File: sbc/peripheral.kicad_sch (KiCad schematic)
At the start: 19 parts, among them J1 Controller-Connector, J2 Controller-Connector, J3 SIO-Header, J4 QTPY-RP2040, U12 TXU0104, U13 TXU0204

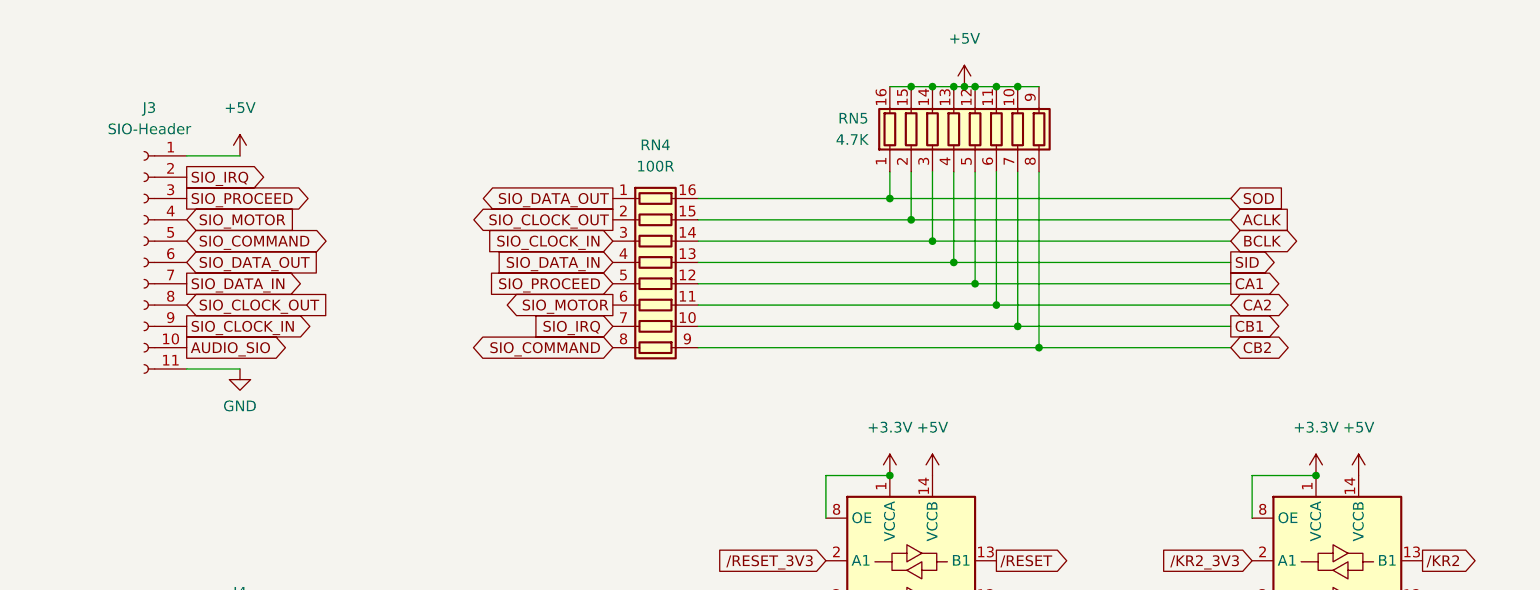
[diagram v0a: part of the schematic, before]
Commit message: SBC v1.1
PCB fixes/changes:

  - Permanently power voltage translators
  - Conservatively specified a slower SRAM (the previous/faster SRAM does actually work fine)
  - RMU: Speculatively provided unbuffered PHI0 input and OE output (not actually needed)
  - Add pullups to open drain GTIA outputs
  - Plot selected values on silk screen
  - Accommodate KiCad 7 upgrade

- PLD changes:
  - Fix AMU logic
  - Fix RMU (unbuffered PHI0 and OE output not needed)

- QTPY firmware:
  - add soft power on/off support (Ctrl-F12)
  - reflects switched power and usb state in the neopixel
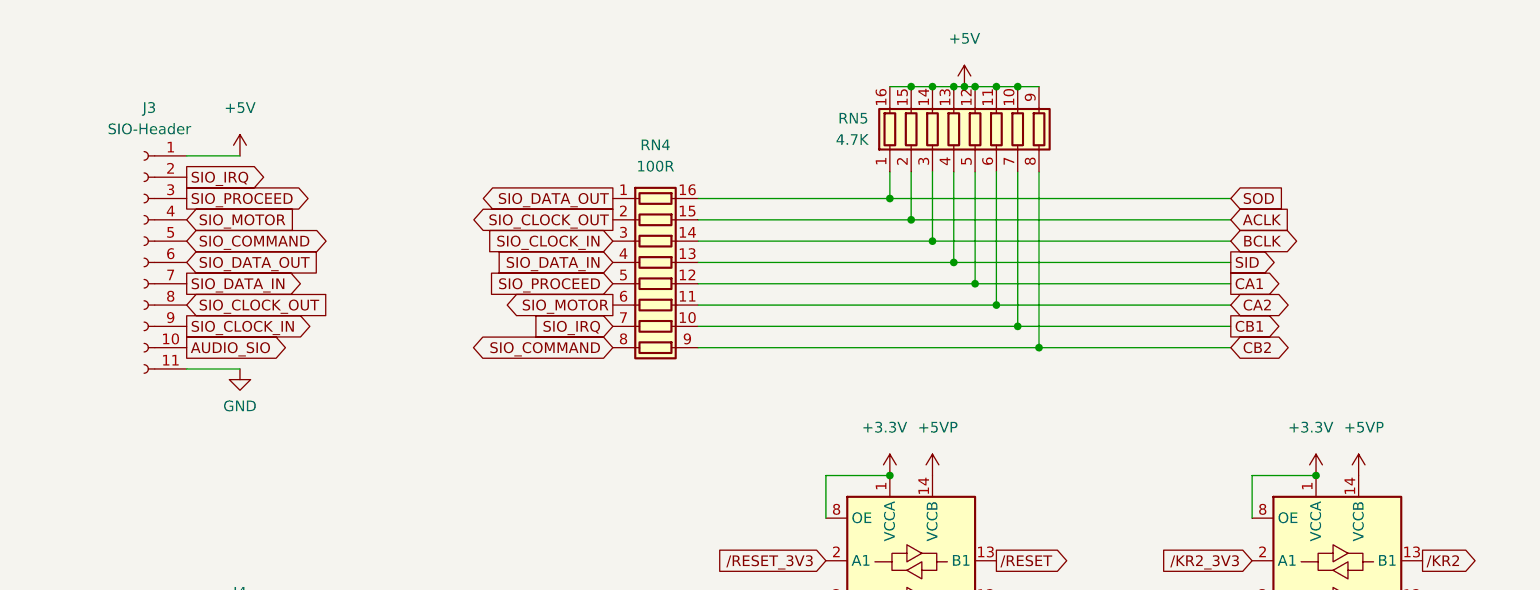
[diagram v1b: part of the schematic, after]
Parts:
- J1, J2: symbol Connector:DB9_Male_MountingHoles -> Connector:DE9_Plug_MountingHoles
- J3: symbol Connector:Conn_01x11_Female -> Connector:Conn_01x11_Socket
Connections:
- net +5V: no longer U12.14 (VCCB), U13.14 (VCCB)
- net +5VP: now also U12.14 (VCCB), U13.14 (VCCB)
- net +3V3 renamed +3.3V

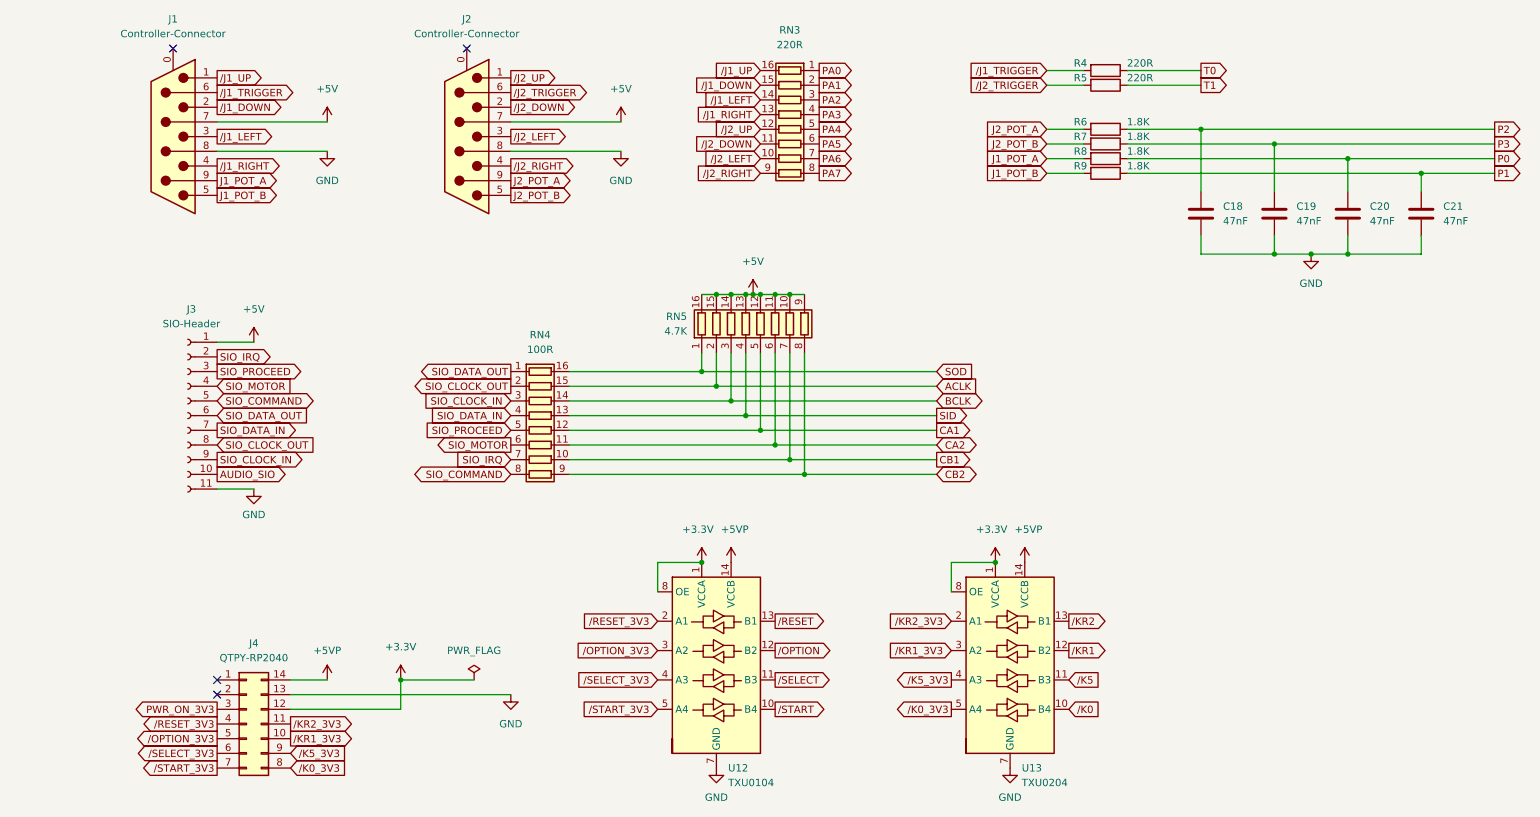
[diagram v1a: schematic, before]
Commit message: SBC v1.2
SBC fixes/changes:

  - S-Video:
    - Fix S-Video footprint (Y and C swapped, and GNDs swapped) and adapt schematic to match
    - Wire S-Video grounds to AVA header instead of directly to (digital) GND
  - Audio:
    - Wire Audio-Out ground to AVA header
    - Drop SIO audio
    - Pullup open drain pokey audio
  - AMU/RMU:
    - Connect ROM and RAM OE to GND
    - Reserve AMU pin for "IO"
    - Reserve RMU pin for "antic" (registered halt)
    - Support for separate Antic banking (clock RMU with /phi2)
    - Supoprt 130XE and 320XE (compy)
  - Add the option for a resistor between OSC, PHI0 buffer and PHI2 buffer (to reduce over/under-shoot)
  - Invert CA2 (a PNP transistor on the Atari 800 XL inverts this signal)

Additions:

  - SBC Audio/Video board
  - SBC Case
  - SBC SD board

Stylize the complete system as "SFF 320XE".
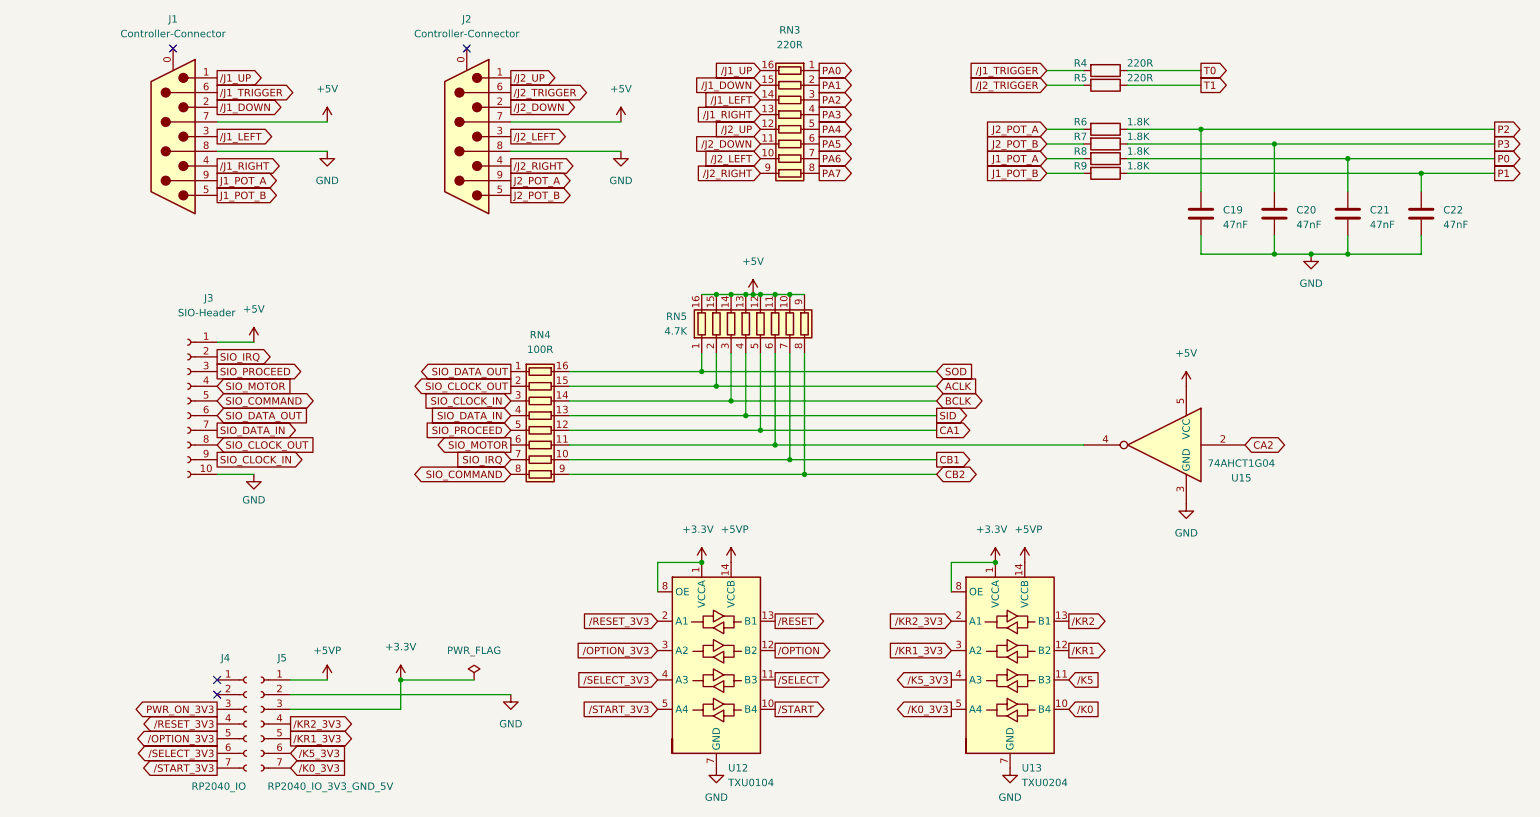
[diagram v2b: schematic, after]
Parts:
- removed J3: SIO-Header, Connector_PinSocket_2.54mm:PinSocket_1x11_P2.54mm_Vertical, symbol Connector:Conn_01x11_Socket
- removed J4: QTPY-RP2040, Package_DIP:DIP-14_W15.24mm, symbol Connector_Generic:Conn_02x07_Counter_Clockwise
- added J3: SIO-Header, Connector_PinSocket_2.54mm:PinSocket_1x10_P2.54mm_Vertical, symbol Connector:Conn_01x10_Socket
- added J4: RP2040_IO, Connector_PinSocket_2.54mm:PinSocket_1x07_P2.54mm_Vertical, symbol Connector:Conn_01x07_Socket
- added J5: RP2040_IO_3V3_GND_5V, Connector_PinSocket_2.54mm:PinSocket_1x07_P2.54mm_Vertical, symbol Connector:Conn_01x07_Socket
- added U15: 74AHCT1G04, Package_TO_SOT_SMD:SOT-23-5_HandSoldering, symbol 74xGxx:74AHCT1G04
- renumbered C18 to C19, C19 to C20, C20 to C21, C21 to C22
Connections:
- net +3.3V: now also J5.3 (Pin_3)
- net +5V: now also J3.1 (Pin_1), U15.5 (VCC)
- net +5VP: now also J5.1 (Pin_1)
- net CA2: now also U15.2; no longer RN4.11 (R6.2), RN5.6 (R6.1)
- net GND: now also J3.10 (Pin_10), J5.2 (Pin_2), U15.3 (GND)
- net PWR_ON_3V3: now also J4.3 (Pin_3)
- net SIO_CLOCK_IN: now also J3.9 (Pin_9)
- net SIO_CLOCK_OUT: now also J3.8 (Pin_8)
- net SIO_COMMAND: now also J3.5 (Pin_5)
- net SIO_DATA_IN: now also J3.7 (Pin_7)
- net SIO_DATA_OUT: now also J3.6 (Pin_6)
- net SIO_IRQ: now also J3.2 (Pin_2)
- net SIO_MOTOR: now also J3.4 (Pin_4)
- net SIO_PROCEED: now also J3.3 (Pin_3)
- net /K0_3V3: now also J5.7 (Pin_7)
- net /K5_3V3: now also J5.6 (Pin_6)
- net /KR1_3V3: now also J5.5 (Pin_5)
- net /KR2_3V3: now also J5.4 (Pin_4)
- net /OPTION_3V3: now also J4.5 (Pin_5)
- net /RESET_3V3: now also J4.4 (Pin_4)
- net /SELECT_3V3: now also J4.6 (Pin_6)
- net /START_3V3: now also J4.7 (Pin_7)
- new net: RN4.11 (R6.2), RN5.6 (R6.1), U15.4

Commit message: SBC v1.3
Motherboard updates:

  - KiCad 9 upgrade
  - USB-C power connector
  - Replace EOL resistor packs with discrete SMD resistors
  - Power/enable voltage translators from switched 5V
  - Fix motor signal pullup
  - Eliminate loop in phi2 traces
  - Thicker clock signal traces

SD card adapter updates:

  - KiCad 9 upgrade
  - Power/enable voltage translator from switched 5V and the eliminate unnecessary SIO pullups

Audio/Video adapter updates:

  - KiCad 9 upgrade
  - No functional changes, gerbers not regenerated, cleaned up bom
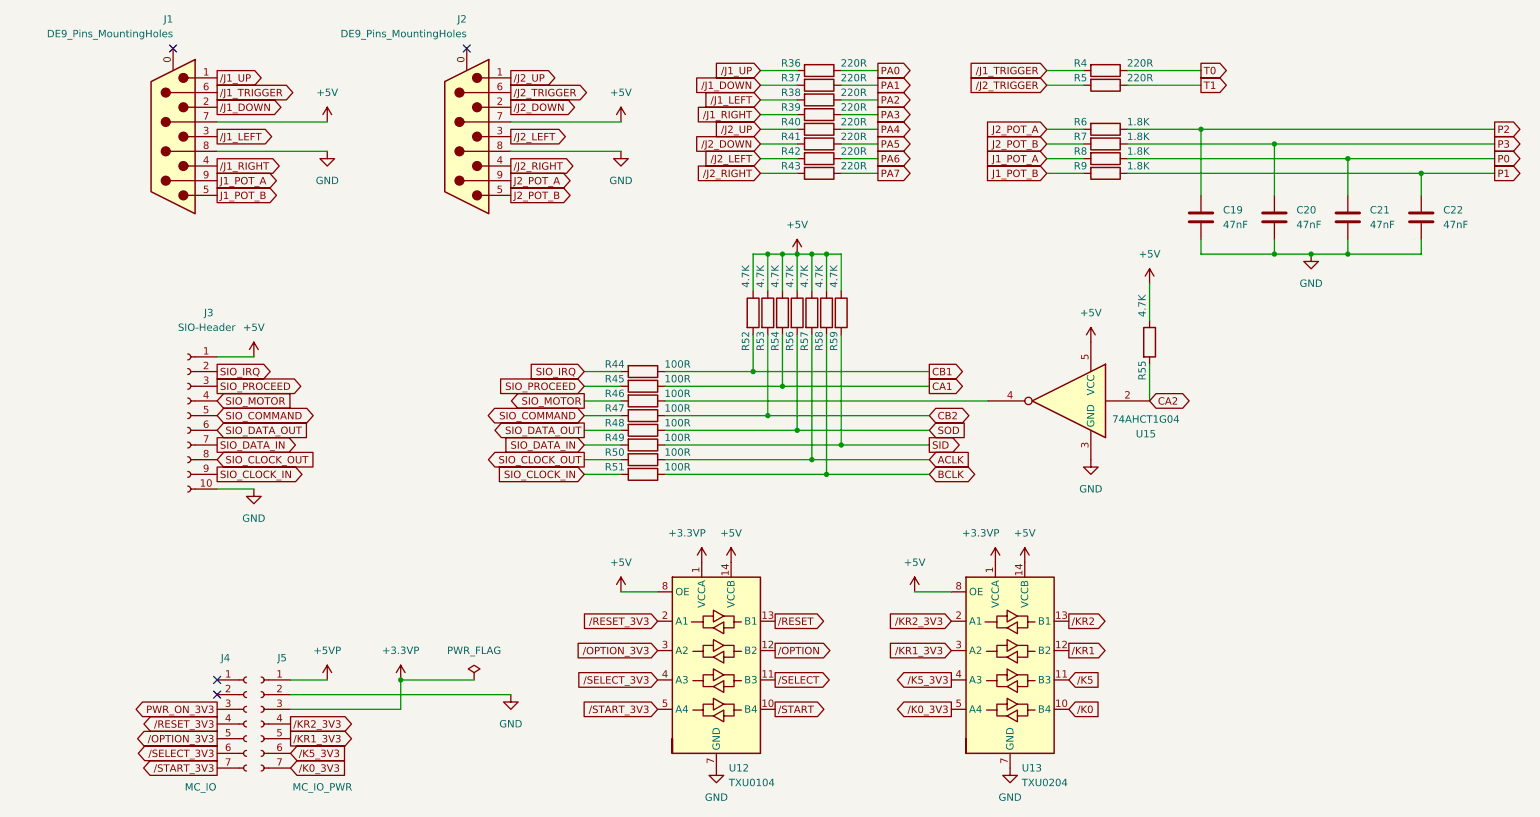
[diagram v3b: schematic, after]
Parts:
- removed J1, J2: Controller-Connector, Project_Connector_Dsub:DSUB-9_Male_Horizontal_PDI-09S-5-RG30, symbol Connector:DE9_Plug_MountingHoles
- removed RN3: 220R, Package_SO:SOIC-16_3.9x9.9mm_P1.27mm, symbol Device:R_Pack08
- removed RN4: 100R, Package_SO:SOIC-16_3.9x9.9mm_P1.27mm, symbol Device:R_Pack08
- removed RN5: 4.7K, Package_SO:SOIC-16_3.9x9.9mm_P1.27mm, symbol Device:R_Pack08
- added J1, J2: DE9_Pins_MountingHoles, Connector_Dsub:DSUB-9_Pins_Horizontal_P2.77x2.84mm_EdgePinOffset4.94mm_Housed_MountingHolesOffset4.94mm, symbol Connector:DE9_Pins_MountingHoles
- added R36, R37, R38, R39, R40, R41, R42, R43: 220R, Resistor_SMD:R_0805_2012Metric_Pad1.20x1.40mm_HandSolder, symbol Device:R
- added R44, R45, R46, R47, R48, R49, R50, R51: 100R, Resistor_SMD:R_0805_2012Metric_Pad1.20x1.40mm_HandSolder, symbol Device:R
- added R52, R53, R54, R55, R56, R57, R58, R59: 4.7K, Resistor_SMD:R_0805_2012Metric_Pad1.20x1.40mm_HandSolder, symbol Device:R
- J4: value RP2040_IO -> MC_IO
- J5: value RP2040_IO_3V3_GND_5V -> MC_IO_PWR
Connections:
- net +5V: now also U12.14 (VCCB), U12.8 (OE), U13.14 (VCCB), U13.8 (OE), J1.7, J2.7, R52.1, R53.1, R54.1, R55.1, R56.1, R57.1, R58.1, R59.1
- net +5VP: no longer U12.14 (VCCB), U13.14 (VCCB)
- net ACLK: now also R50.1, R57.2
- net BCLK: now also R51.1, R58.2
- net CA1: now also R45.1, R54.2
- net CA2: now also R55.2
- net CB1: now also R44.1, R52.2
- net CB2: now also R47.1, R53.2
- net GND: now also J1.8, J2.8
- net J1_POT_A: now also J1.9
- net J1_POT_B: now also J1.5
- net J2_POT_A: now also J2.9
- net J2_POT_B: now also J2.5
- net PA0: now also R36.1
- net PA1: now also R37.1
- net PA2: now also R38.1
- net PA3: now also R39.1
- net PA4: now also R40.1
- net PA5: now also R41.1
- net PA6: now also R42.1
- net PA7: now also R43.1
- net SID: now also R49.1, R59.2
- net SIO_CLOCK_IN: now also R51.2
- net SIO_CLOCK_OUT: now also R50.2
- net SIO_COMMAND: now also R47.2
- net SIO_DATA_IN: now also R49.2
- net SIO_DATA_OUT: now also R48.2
- net SIO_IRQ: now also R44.2
- net SIO_MOTOR: now also R46.2
- net SIO_PROCEED: now also R45.2
- net SOD: now also R48.1, R56.2
- net /J1_DOWN: now also J1.2, R37.2
- net /J1_LEFT: now also J1.3, R38.2
- net /J1_RIGHT: now also J1.4, R39.2
- net /J1_TRIGGER: now also J1.6
- net /J1_UP: now also J1.1, R36.2
- net /J2_DOWN: now also J2.2, R41.2
- net /J2_LEFT: now also J2.3, R42.2
- net /J2_RIGHT: now also J2.4, R43.2
- net /J2_TRIGGER: now also J2.6
- net /J2_UP: now also J2.1, R40.2
- net at U15.4: now also R46.1
- net +3.3V renamed +3.3VP
- net +3.3VP: no longer U12.8 (OE), U13.8 (OE)
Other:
- moved on the sheet: C19, C20, C21, C22, J3, U15
